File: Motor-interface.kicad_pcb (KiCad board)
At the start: 2 copper layers, 69 parts, among them J101 0, J102 0, J201 RJ45, J202 RJ45, P101 TE-23pins connector, P102 PSU_ISO, P103 Halls, P104 LineContactor, P105 ReverseContactor, P106 FanContactor, P107 Battery+, P108 MC_USB, P109 MC_CAN, Q101 Q_NPN_BCE, U101 AP1117D50, U102 AP1117D33, U103 TLP2361, U104 TLP2361, U105 TLP2361, U106 TLP2361, U107 TLP2361, U108 TLP2361, U109 Teensy_3.2, U110 TLP2361, U111 FODM3052, U201 TLP2361, U202 TLP2361, U203 MCP2551-I/SN, U301 MCP4251, U302 TLP2361, U303 TLP2361, U304 TLP2361, U305 TLP2361, U306 TLP290-4

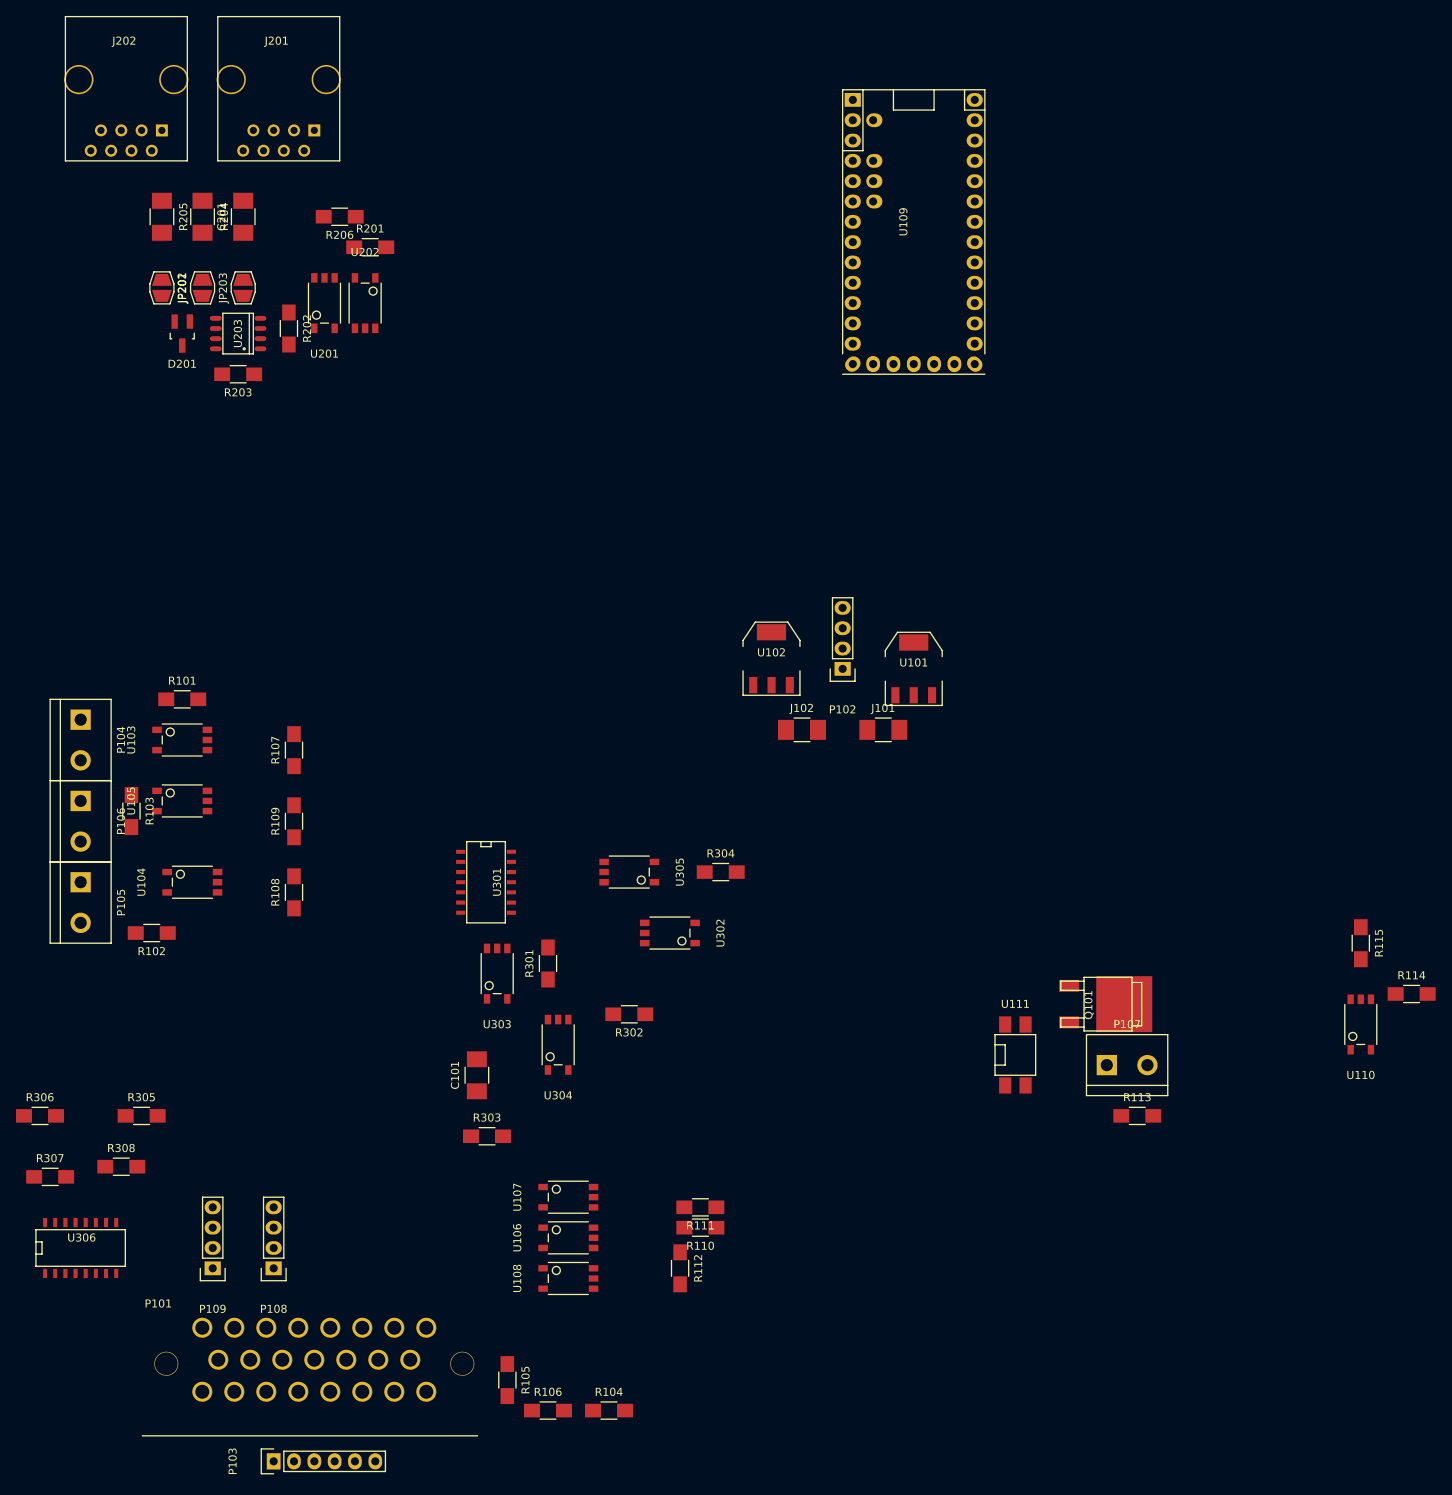
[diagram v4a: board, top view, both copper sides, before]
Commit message: swapped pins, arranged parts
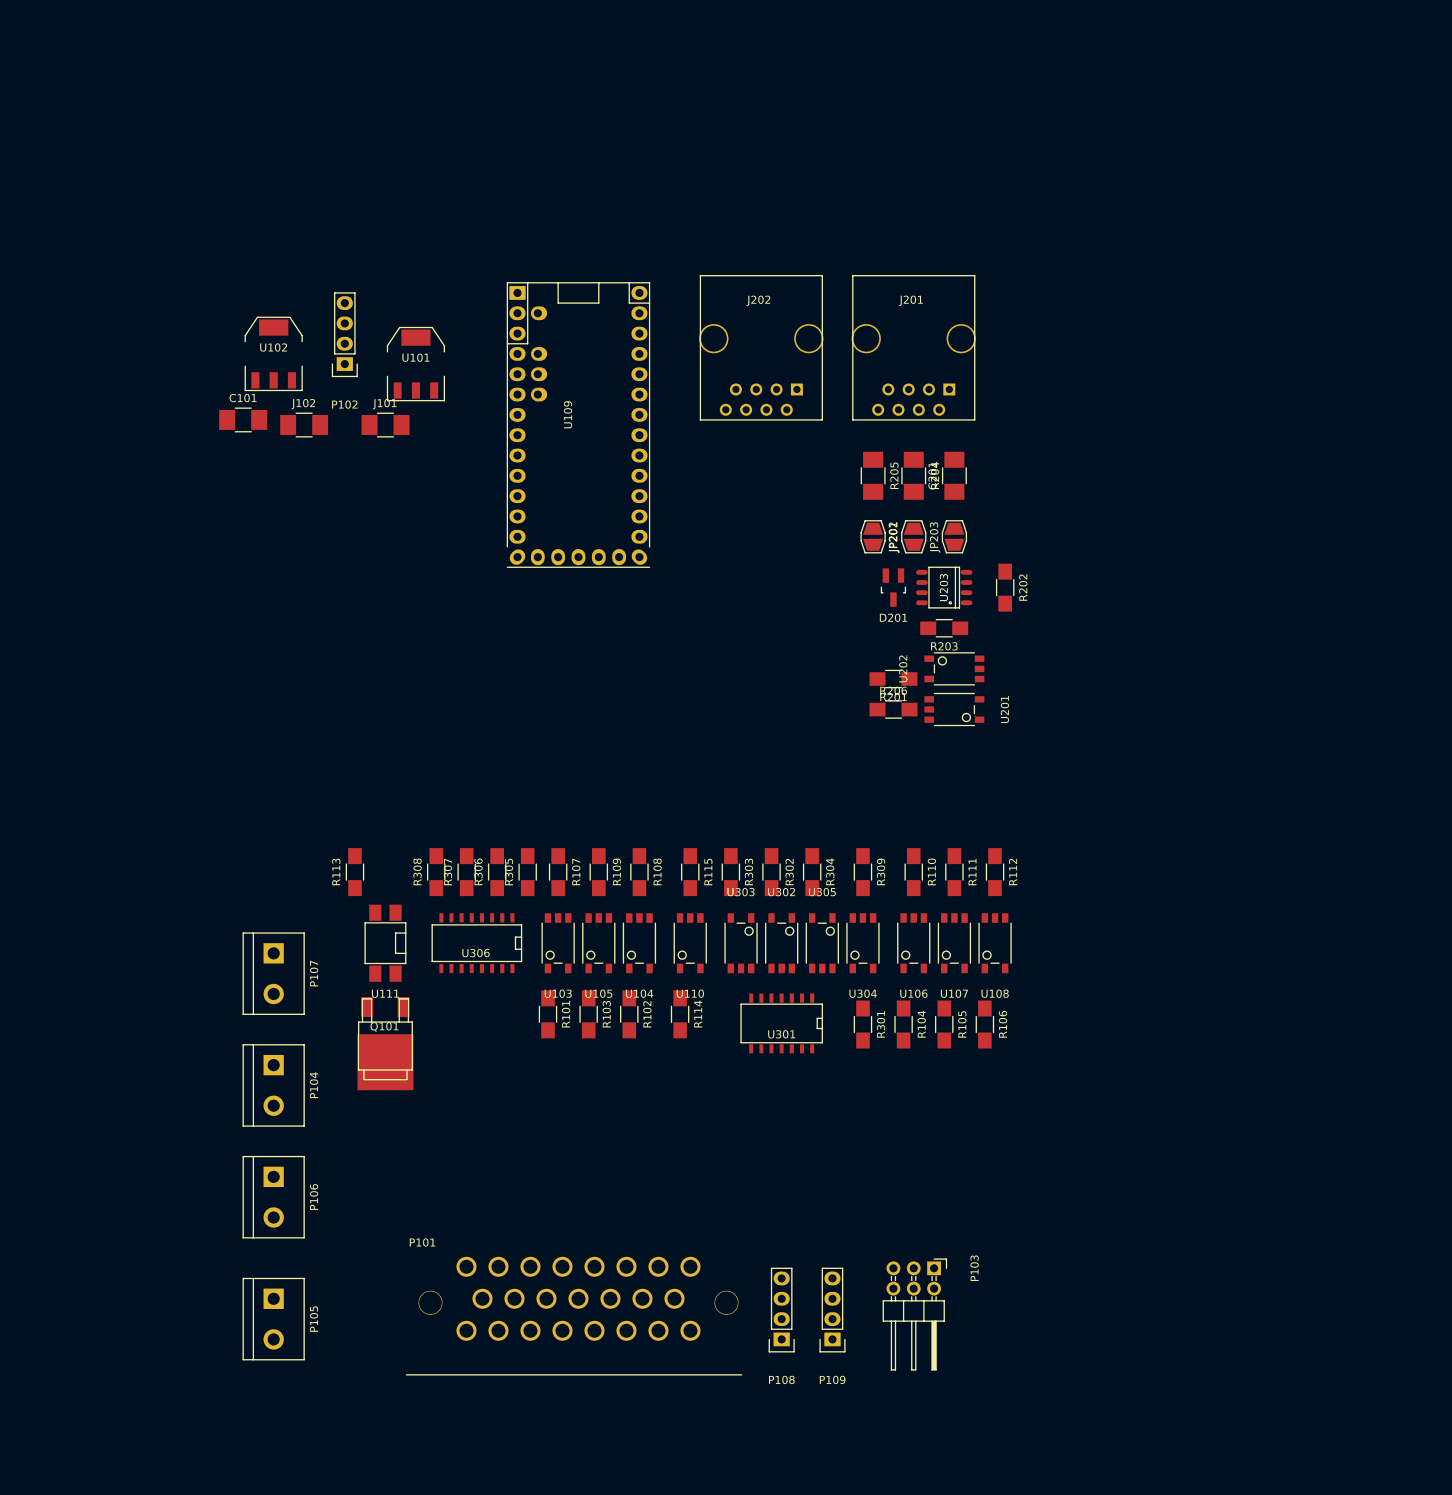
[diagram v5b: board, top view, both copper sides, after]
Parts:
- added R309: 1k, Resistors_SMD:R_1206_HandSoldering, F.Cu at (121.9, 121.9)
- P103: footprint Pin_Headers:Pin_Header_Straight_1x06 -> Pin_Headers:Pin_Header_Angled_2x03
- moved P107 107.3 mm to (48.3, 134.6), turned to 270 degrees
- moved R113 102.4 mm to (58.4, 121.9), turned to 90 degrees
- moved R202 95.2 mm to (139.7, 86.4)
- moved R204 94.6 mm to (128.3, 72.4)
- moved R205 94.6 mm to (123.2, 72.4)
- moved C201 94.6 mm to (133.3, 72.4)
- moved D201 94.4 mm to (125.7, 86.4)
- moved JP201 94.2 mm to (128.3, 80.0)
- moved JP202 94.2 mm to (123.2, 80.0)
- moved JP203 94.2 mm to (133.3, 80.0)
- moved R203 93.8 mm to (132.1, 91.4)
- moved U203 93.8 mm to (132.1, 86.4)
- moved U201 93.7 mm to (133.3, 101.6), turned to 90 degrees
- moved R206 92.7 mm to (125.7, 101.6), turned to 0 degrees
- moved R114 91.5 mm to (99.1, 139.7), turned to 270 degrees
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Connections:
- P101 pad 8: GND -> /PotsSwitches/Motor_GND
- P103 pad 1: /Motor-sensor-A -> /Motor-sensor-C
- P103 pad 2: /Motor-sensor-B -> /Motor-temperature
- P103 pad 3: /Motor-sensor-C -> /Motor-sensor-B
- P103 pad 4: /Hall_Power -> /Hall_GND
- P103 pad 5: /Hall_GND -> /Motor-sensor-A
- P103 pad 6: /Motor-temperature -> /Hall_Power
- P108 pad 3: GND -> /PotsSwitches/Motor_GND
- P109 pad 3: GND -> /PotsSwitches/Motor_GND
- U110 pad 3: GND -> /PotsSwitches/Motor_GND
- U301 pad 10: GND -> /PotsSwitches/Motor_GND
- U301 pad 14: /PotsSwitches/Motor_5V -> /PotsSwitches/+5V
- U301 pad 4: GND -> /PotsSwitches/Motor_GND
- U301 pad 5: GND -> /PotsSwitches/Motor_GND
- U301 pad 6: /PotsSwitches/AccelPot -> /PotsSwitches/BrakePot
- U301 pad 9: /PotsSwitches/BrakePot -> /PotsSwitches/AccelPot
- U302 pad 4: GND -> /PotsSwitches/Motor_GND
- U303 pad 4: GND -> /PotsSwitches/Motor_GND
- U304 pad 5: /PotsSwitches/MISO -> Net-(R309-Pad2)
- U305 pad 4: GND -> /PotsSwitches/Motor_GND
- U306 pad 11: GND -> /PotsSwitches/Motor_GND
- U306 pad 13: GND -> /PotsSwitches/Motor_GND
- U306 pad 15: GND -> /PotsSwitches/Motor_GND
- U306 pad 9: GND -> /PotsSwitches/Motor_GND

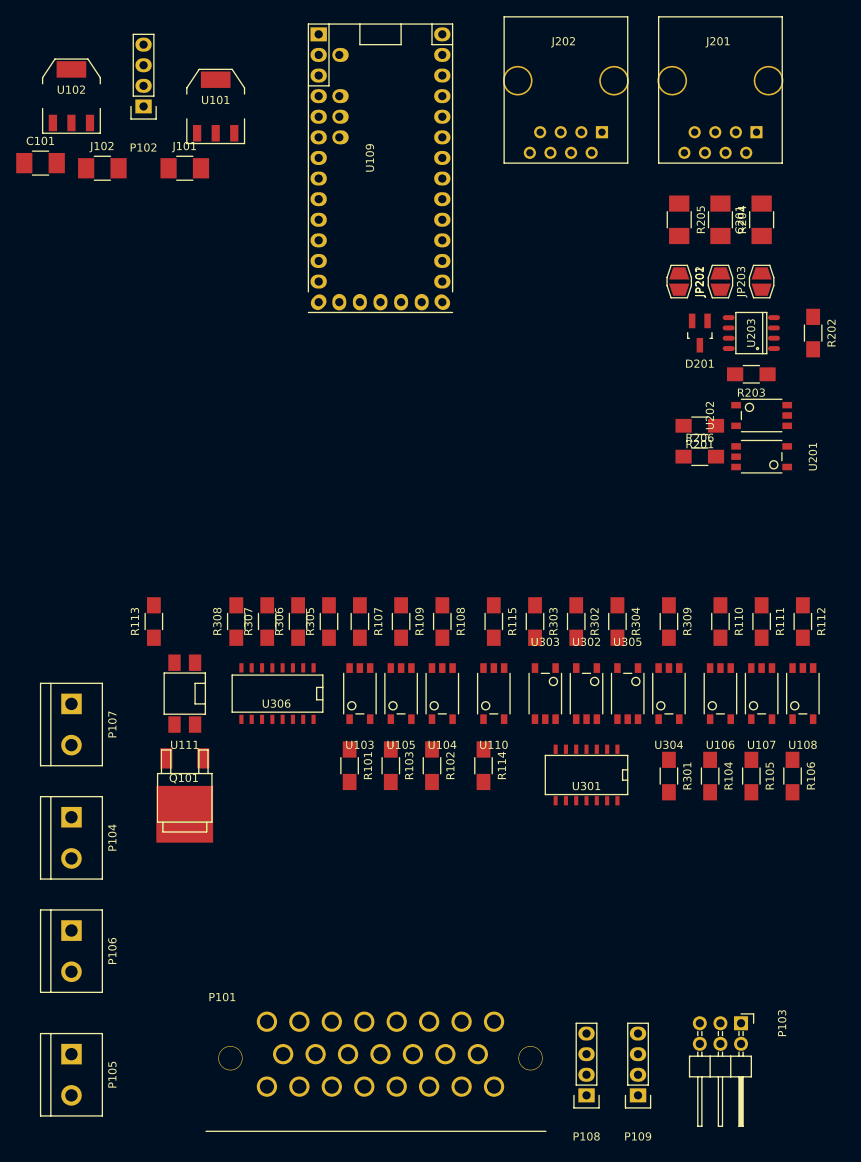
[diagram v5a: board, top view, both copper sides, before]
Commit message: laid out CAN hardware
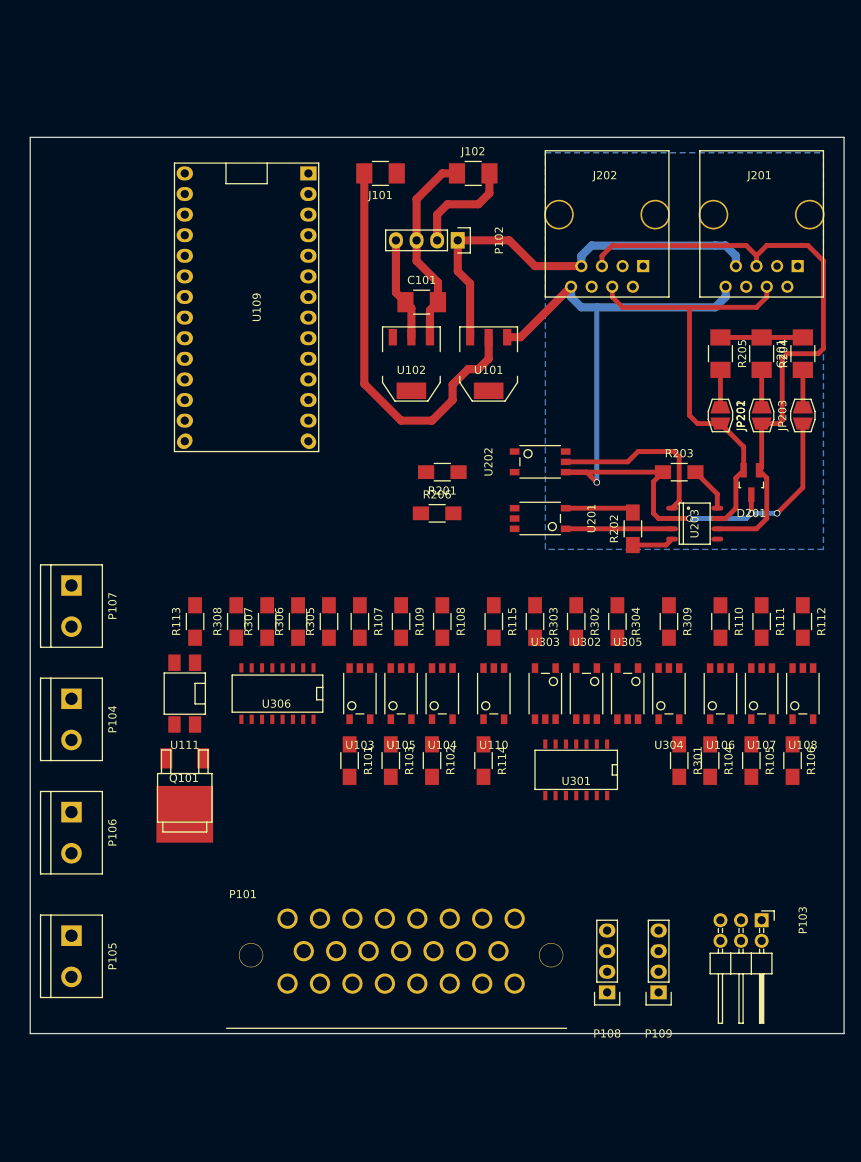
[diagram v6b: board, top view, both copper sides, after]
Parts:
- U109: footprint electric_car_lib:Teensy3.2_inv -> electric_car_lib:Teensy3.2
- moved U102 53.4 mm to (90.2, 90.2), turned to 180 degrees
- moved C101 50.0 mm to (91.4, 82.5)
- moved U101 46.3 mm to (99.7, 90.2), turned to 180 degrees
- moved J102 45.7 mm to (97.8, 66.7)
- moved P102 42.1 mm to (95.9, 74.9), turned to 270 degrees
- moved R206 33.1 mm to (93.3, 108.6)
- moved R202 32.8 mm to (117.5, 110.5), turned to 90 degrees
- moved R201 32.3 mm to (94.0, 103.5)
- moved U201 28.3 mm to (106.0, 109.2)
- moved U202 27.9 mm to (106.0, 102.2)
- moved U203 24.5 mm to (125.1, 109.9), turned to 270 degrees
- moved J101 24.1 mm to (86.4, 66.7), turned to 180 degrees
- moved U109 23.8 mm to (69.8, 83.2)
- moved D201 19.5 mm to (132.1, 104.8)
- moved C201 17.3 mm to (138.4, 88.9)
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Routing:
- net GNDA: track 0.00 -> 120.3 mm, vias 0 -> 4
- net /CANmodule/CAN_L: track 0.00 -> 77.8 mm
- net +5VA: track 0.00 -> 63.2 mm
- net /CANmodule/CAN_H: track 0.00 -> 56.0 mm
- net +12V: track 0.00 -> 52.3 mm
- net GND: track 0.00 -> 24.8 mm
- net Net-(U202-Pad5): track 0.00 -> 21.5 mm
- net +3V3: track 0.00 -> 12.7 mm
- net Net-(C201-Pad2): track 0.00 -> 10.2 mm
- net Net-(R202-Pad2): track 0.00 -> 8.50 mm
- net Net-(R203-Pad2): track 0.00 -> 5.56 mm
- net Net-(R202-Pad1): track 0.00 -> 5.13 mm
- net Net-(JP202-Pad2): track 0.00 -> 4.62 mm
- net Net-(JP201-Pad1): track 0.00 -> 4.62 mm
- net Net-(C201-Pad1): track 0.00 -> 4.62 mm
- added copper zone on B.Cu, net GNDA
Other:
- board outline added: 100.3 x 110.5 mm

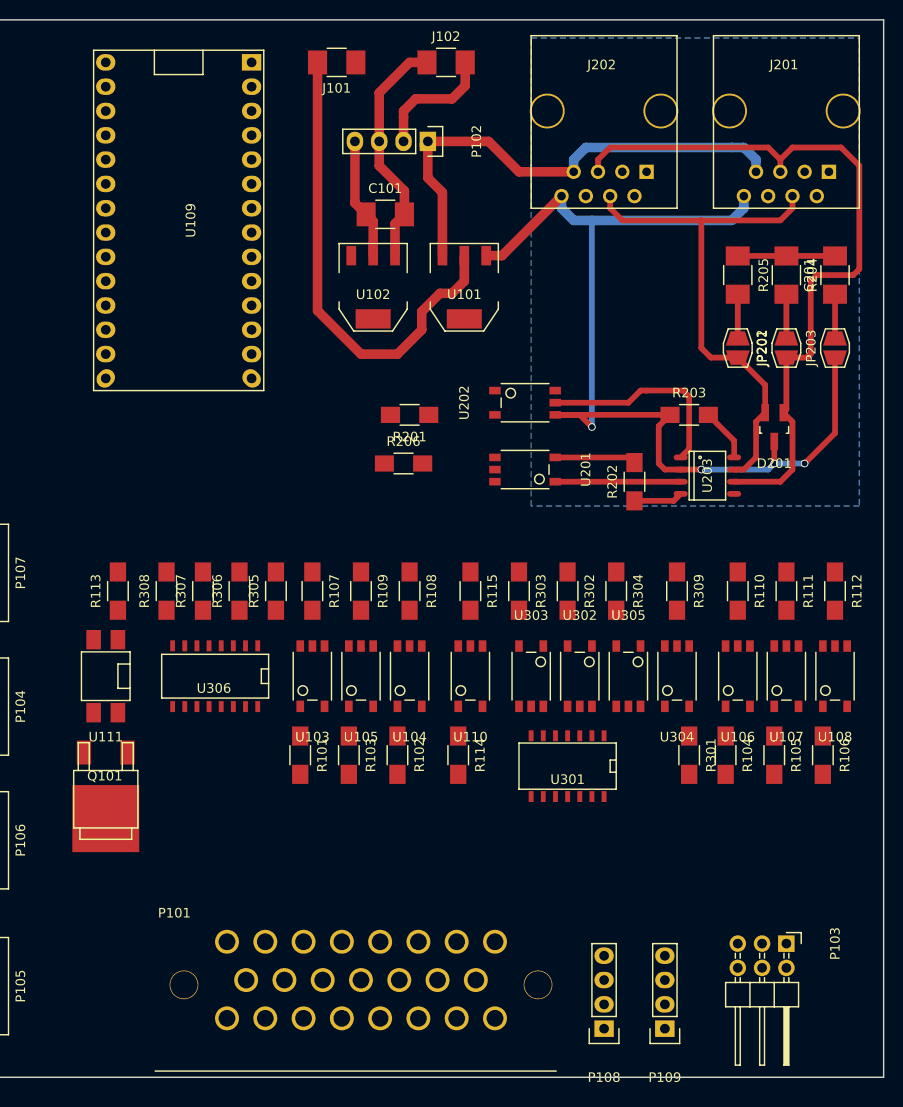
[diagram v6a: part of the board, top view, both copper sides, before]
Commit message: laid out halls and pots
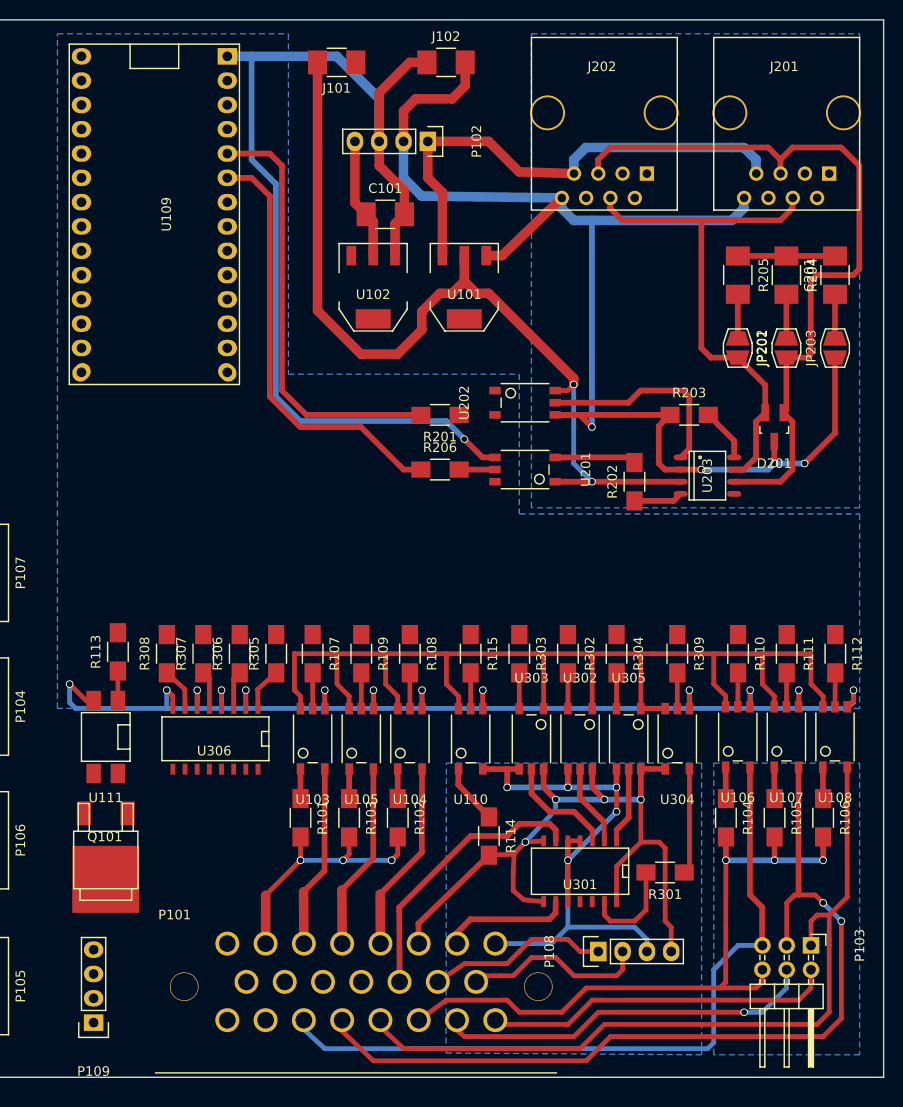
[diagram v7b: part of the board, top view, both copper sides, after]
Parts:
- moved P109 59.7 mm to (61.0, 167.0)
- moved R301 12.5 mm to (120.7, 151.3), turned to 180 degrees
- moved U301 11.1 mm to (111.8, 151.3)
- moved R114 9.03 mm to (102.3, 147.5)
- moved P108 8.09 mm to (113.7, 159.6), turned to 90 degrees
- moved R107 6.54 mm to (83.8, 128.5)
- moved R108 6.54 mm to (94.0, 128.5)
- moved R109 6.54 mm to (88.9, 128.5)
- moved R110 6.54 mm to (128.3, 128.5)
- moved R111 6.54 mm to (133.4, 128.5)
- moved R112 6.54 mm to (138.5, 128.5)
- moved R115 6.54 mm to (100.4, 128.5)
- moved R302 6.54 mm to (110.5, 128.5)
- moved R303 6.54 mm to (105.4, 128.5)
- moved R304 6.54 mm to (115.6, 128.5)
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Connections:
- U301 pad 14: /PotsSwitches/+5V -> /PotsSwitches/Motor_5V
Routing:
- net GND: track 24.8 -> 242.0 mm, vias 0 -> 14
- net +3V3: track 12.7 -> 129.5 mm
- net /Motor-sensor-B: track 0.00 -> 91.6 mm, vias 0 -> 2
- net /Motor-sensor-C: track 0.00 -> 81.2 mm
- net /PotsSwitches/Motor_5V: track 0.00 -> 79.3 mm, vias 0 -> 4
- net /Motor-sensor-A: track 0.00 -> 78.2 mm
- net /Hall_Power: track 0.00 -> 70.3 mm, vias 0 -> 3
- net /PotsSwitches/Motor_GND: track 0.00 -> 65.8 mm, vias 0 -> 5
- net /CANmodule/CAN_TX: track 0.00 -> 45.3 mm
- net /CANmodule/CAN_RX: track 0.00 -> 45.1 mm
- net /Hall_GND: track 0.00 -> 39.3 mm, vias 0 -> 1
- net /Motor-temperature: track 0.00 -> 36.2 mm
- net +5VA: track 63.2 -> 96.5 mm, vias 0 -> 2
- net /PotsSwitches/BrakePot: track 0.00 -> 29.2 mm
- net /Contactor+Common: track 0.00 -> 27.6 mm, vias 0 -> 3
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- added copper zone on B.Cu, net /Hall_GND
- added copper zone on B.Cu, net /M_GND
- added copper zone on B.Cu, net GND
